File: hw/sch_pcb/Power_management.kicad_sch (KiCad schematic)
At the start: 40 parts

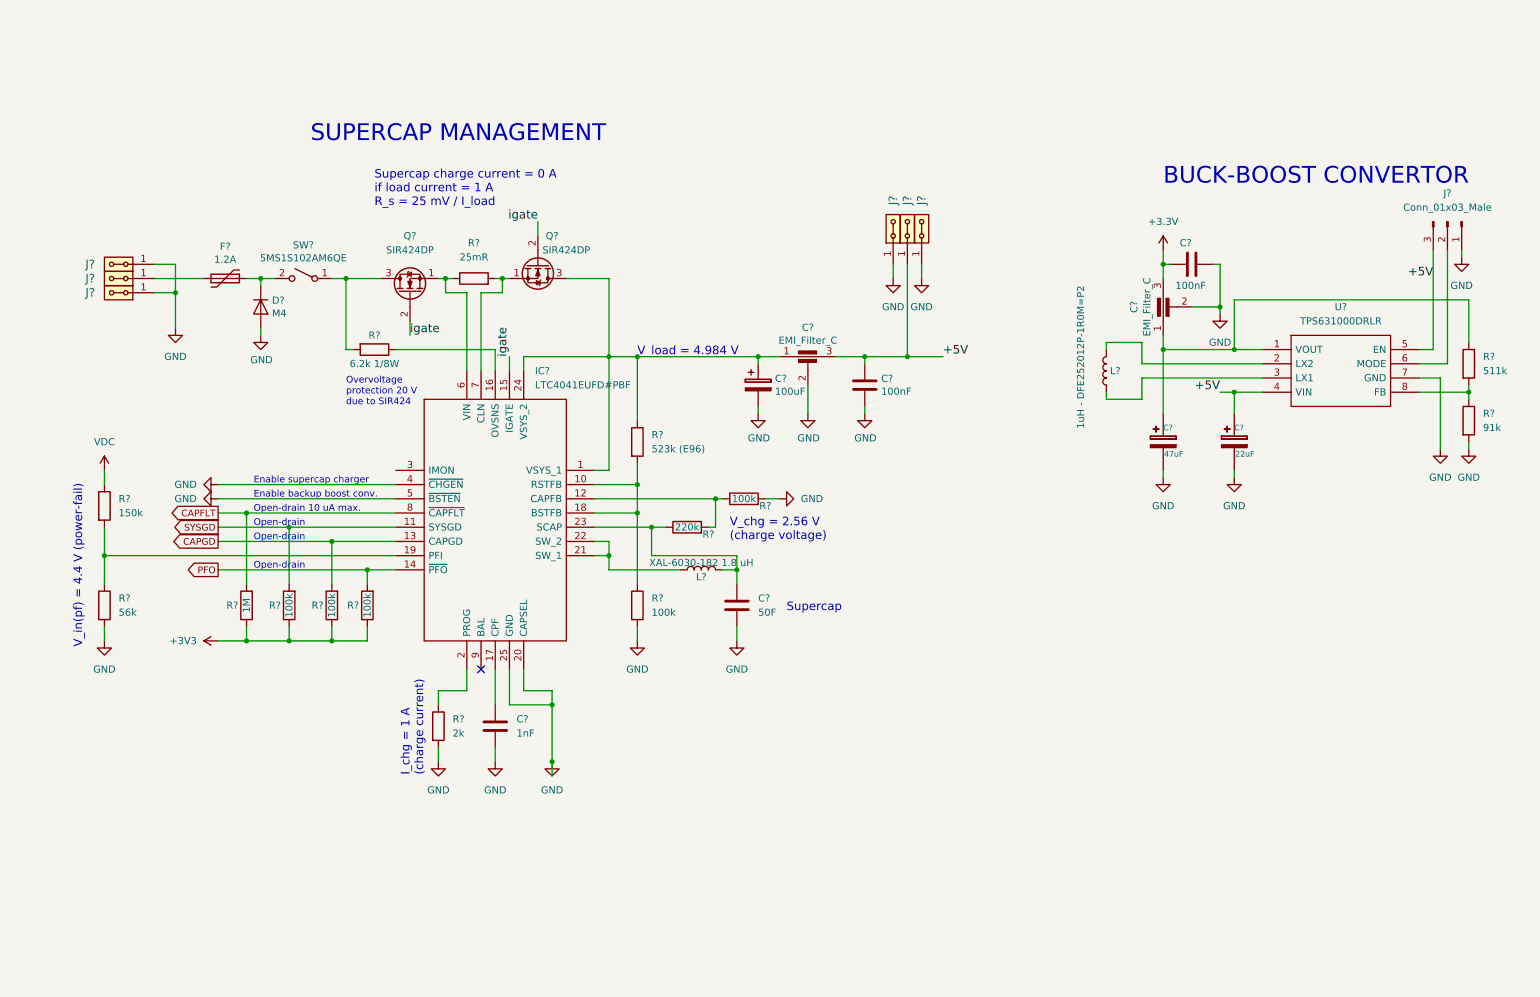
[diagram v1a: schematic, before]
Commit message: schematics update
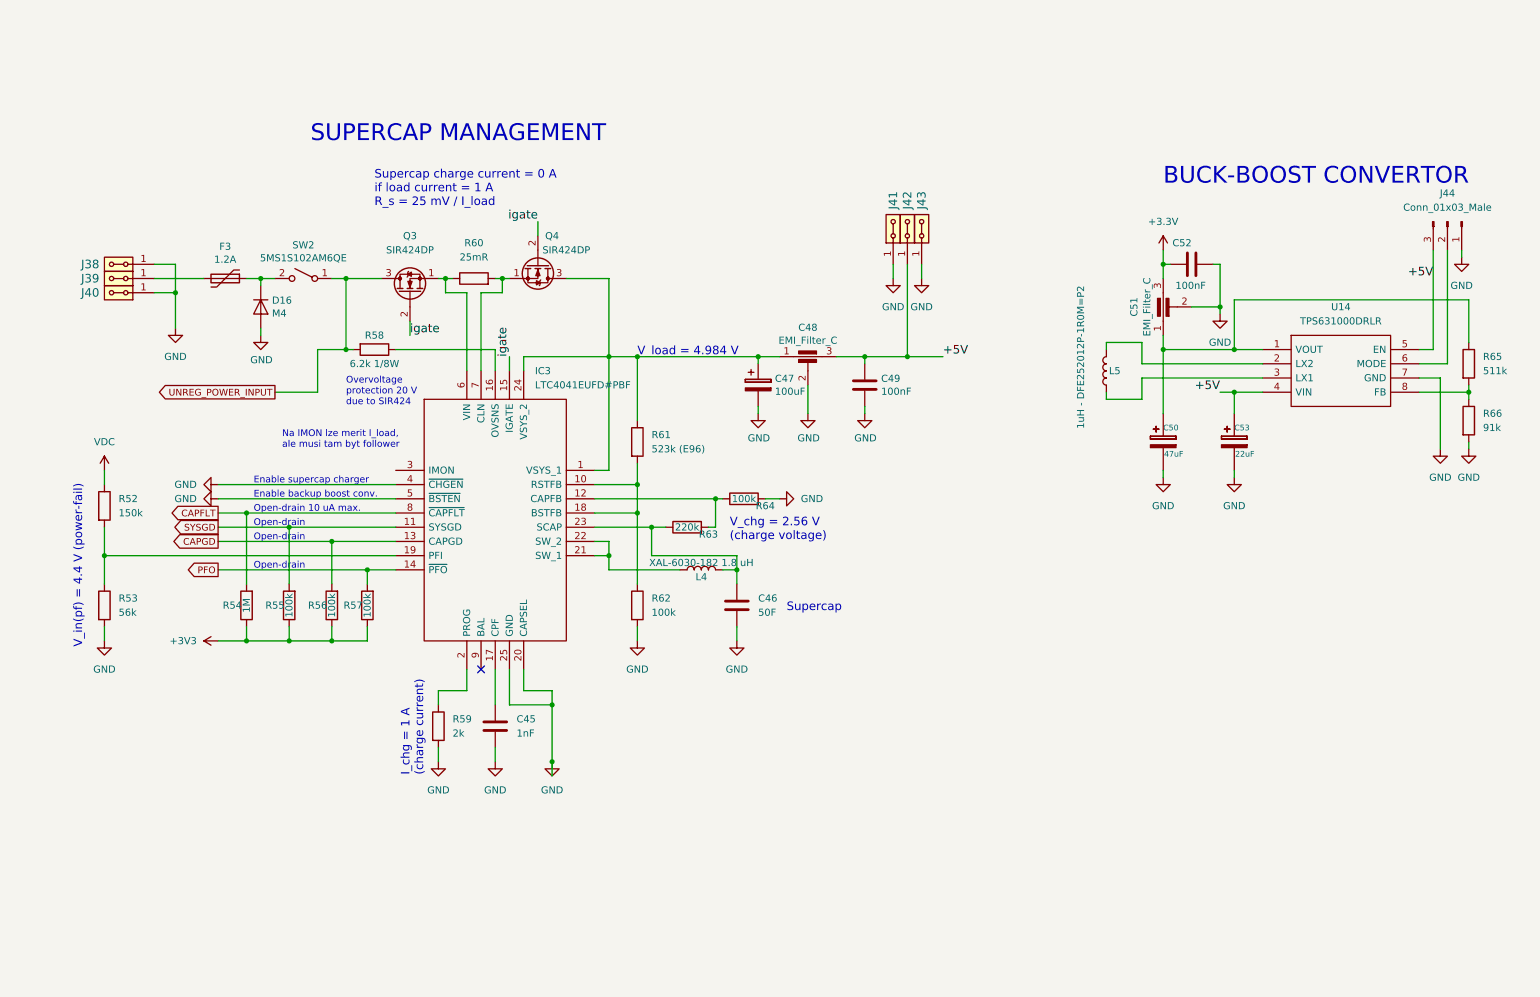
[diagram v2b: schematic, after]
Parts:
- gave numbers to parts that had none: 40
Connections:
- net UNREG_POWER_INPUT: now reaches Q3.3 (D), R58.2, SW2.1 (A)
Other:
- note added: "Na IMON lze merit I_load, ale musi tam byt follower"

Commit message: schematics update
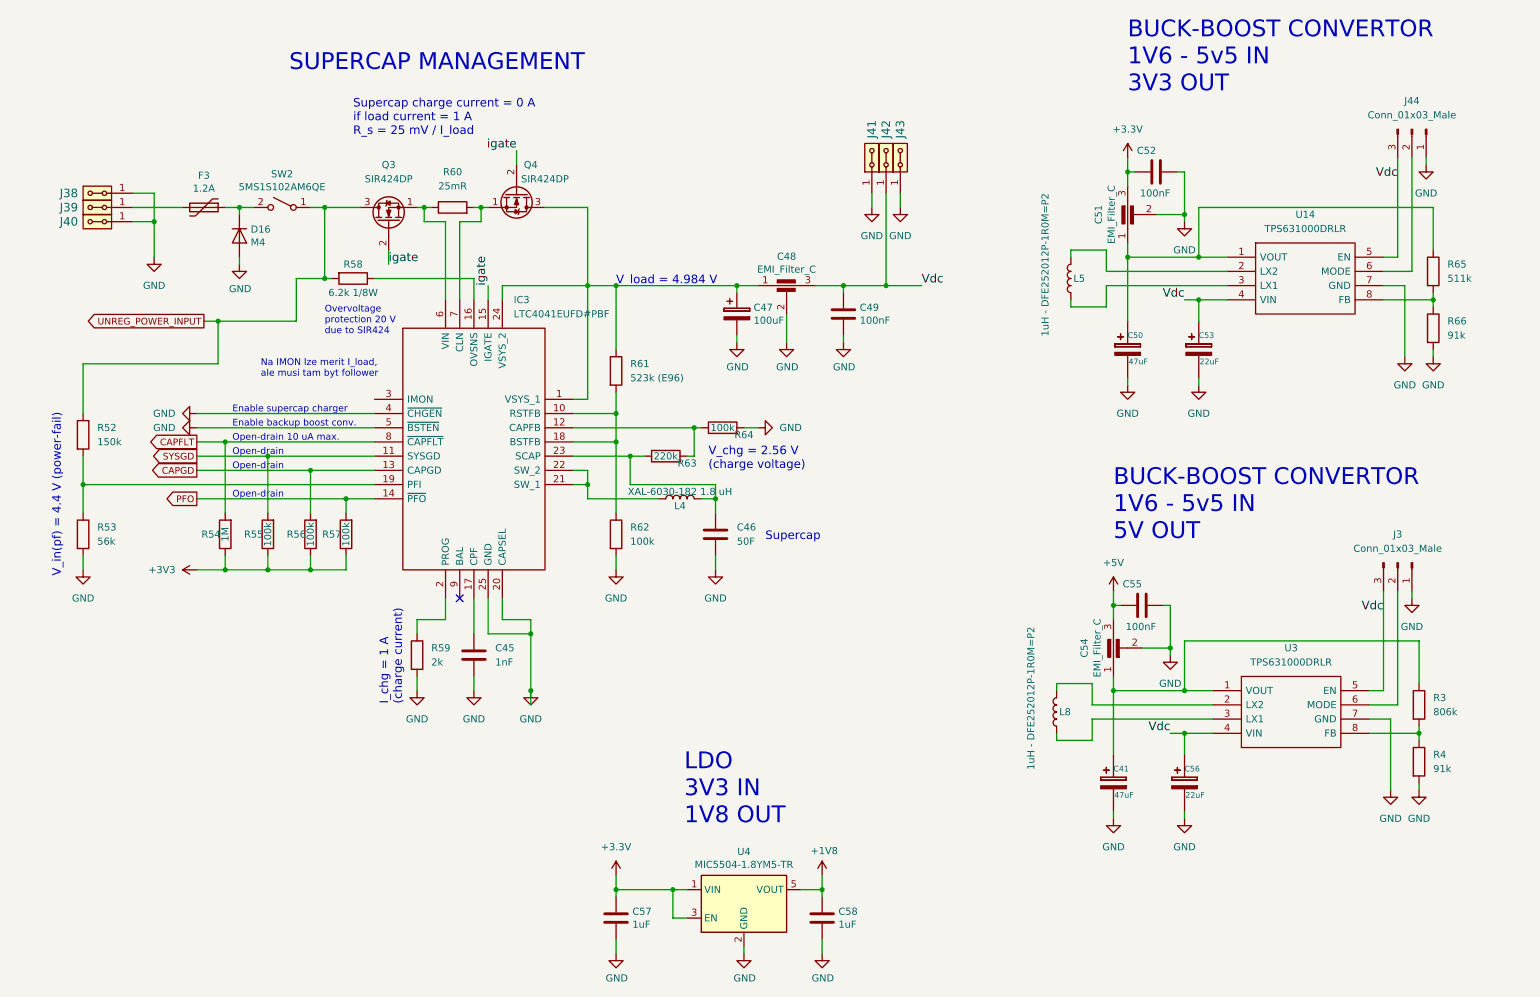
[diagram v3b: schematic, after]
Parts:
- added C41: 47uF, Mlab_C:TantalC_SizeB_Reflow, symbol LION2CELL01D-rescue:CP2
- added C54: EMI_Filter_C, Mlab_L:FIR1, symbol DATALOGGER01A-rescue:EMI_Filter_C-device
- added C55: 100nF, Mlab_R:SMD-0805, symbol DATALOGGER01A-rescue:C-device
- added C56: 22uF, Mlab_C:TantalC_SizeB_Reflow, symbol LION2CELL01D-rescue:CP2
- added C57, C58: 1uF, Mlab_R:SMD-0603, symbol Device:C
- added J3: Conn_01x03_Male, symbol Connector:Conn_01x03_Male
- added L8: 1uH - DFE252012P-1R0M=P2, symbol Device:L
- added R3: 806k, symbol Device:R
- added R4: 91k, symbol Device:R
- added U3: TPS631000DRLR, SOTFL50P160X60-8N, symbol TPS631000DRLR:TPS631000DRLR
- added U4: MIC5504-1.8YM5-TR, Package_TO_SOT_SMD:SOT-23-5, symbol Regulator_Linear:MIC5504-1.8YM5
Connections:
- net VDC is gone; now on net UNREG_POWER_INPUT: R52.1
- net +3.3V: now also C57.1, U4.1 (VIN), U4.3 (EN)
- net +5V: now also C54.3, C55.1; no longer C48.3, C49.1, C53.1, J42.1, J42.2, J44.3 (Pin_3), U14.4 (VIN), U14.5 (EN)
- net GND: now also C41.2, C54.2, C55.2, C56.2, C57.2, C58.2, J3.1 (Pin_1), R4.2, U3.7 (GND), U4.2 (GND)
- new net: C41.1, C54.1, R3.1, U3.1 (VOUT)
- new net: L8.1, U3.3 (LX1)
- new net: L8.2, U3.2 (LX2)
- new net: J3.2 (Pin_2), U3.6 (MODE)
- new net: R3.2, R4.1, U3.8 (FB)
- new net +1V8: C58.1, U4.5 (VOUT)
- new net Vdc: C48.3, C49.1, C53.1, C56.1, J3.3 (Pin_3), J42.1, J42.2, J44.3 (Pin_3), U14.4 (VIN), U14.5 (EN), U3.4 (VIN), U3.5 (EN)
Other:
- note added: "BUCK-BOOST CONVERTOR 1V6 - 5v5 IN 3V3 OUT"
- note added: "BUCK-BOOST CONVERTOR 1V6 - 5v5 IN 5V OUT"
- note added: "LDO 3V3 IN 1V8 OUT"
- note removed: "BUCK-BOOST CONVERTOR"
- moved on the sheet: C45, C46, C47, C48, C49, C50, C51, C52, C53, D16, F3, IC3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

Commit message: progress?
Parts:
- removed J38, J39, J40, J41, J42, J43: HEADER_2x01_PARALLEL, Mlab_Pin_Headers:Straight_2x01, symbol DATALOGGER01A-rescue:HEADER_2x01_PARALLEL-MLAB_HEADER
- removed SW2: 5MS1S102AM6QE, Mlab_SW:5MS1S102AM6QE, symbol Switch:SW_SPST
- added J24, J5: HEADER_2x03_PARALLEL, Mlab_Pin_Headers:Straight_2x03, symbol MLAB_HEADER:HEADER_2x03_PARALLEL
- C26: renamed from C45; footprint (none) -> Mlab_C:SMD-0805
- C27: renamed from C57; footprint Mlab_R:SMD-0603 -> Mlab_C:SMD-0805
- C28: renamed from C46; footprint (none) -> Mlab_C:C_Radial_D16_L25_P7.5
- C30: renamed from C48; footprint Mlab_L:FIR1 -> Mlab_L:FIR_0805
- C31: renamed from C58; footprint Mlab_R:SMD-0603 -> Mlab_C:SMD-0805
- C32: renamed from C49; footprint Mlab_R:SMD-0805 -> Mlab_C:SMD-0805
- C35: renamed from C54; footprint Mlab_L:FIR1 -> Mlab_L:FIR_0805
- C36: renamed from C51; footprint Mlab_L:FIR1 -> Mlab_L:FIR_0805
- C37: renamed from C55; footprint Mlab_R:SMD-0805 -> Mlab_C:SMD-0805
- C38: renamed from C52; footprint Mlab_R:SMD-0805 -> Mlab_C:SMD-0805
- D2: renamed from D16; footprint Mlab_D:SMA_Standard -> Mlab_D:Diode-SMA_Standard
- IC3: footprint QFN50P400X500X80-25N-D -> Package_DFN_QFN:QFN-24-1EP_4x5mm_P0.5mm_EP2.65x3.65mm
- J19: renamed from J3; footprint (none) -> Mlab_Pin_Headers:Straight_1x03
- J20: renamed from J44; footprint (none) -> Mlab_Pin_Headers:Straight_1x03
- L2: renamed from L4; footprint (none) -> XAL6030181MEC:XAL6030181MEC
- L3: renamed from L8; footprint (none) -> Inductor_SMD:L_1008_2520Metric
- L4: renamed from L5; footprint (none) -> Inductor_SMD:L_1008_2520Metric
- Q2: renamed from Q3; footprint Package_TO_SOT_THT:TO-92_Inline -> SIR424DP:SIR106DPT1RE3
- Q3: renamed from Q4; footprint Package_TO_SOT_THT:TO-92_Inline -> SIR424DP:SIR106DPT1RE3
- R29: renamed from R52; footprint (none) -> Mlab_R:SMD-0805
- R30: renamed from R53; footprint (none) -> Mlab_R:SMD-0805
- R31: renamed from R54; footprint (none) -> Mlab_R:SMD-0805
- R32: renamed from R55; footprint (none) -> Mlab_R:SMD-0805
- R33: renamed from R56; footprint (none) -> Mlab_R:SMD-0805
- R34: renamed from R57; footprint (none) -> Mlab_R:SMD-0805
- R35: renamed from R58; footprint (none) -> Mlab_R:SMD-0805
- R36: renamed from R59; footprint (none) -> Mlab_R:SMD-0805
- R37: renamed from R60; footprint (none) -> Mlab_R:SMD-0805
- R38: renamed from R61; footprint (none) -> Mlab_R:SMD-0805
- R39: renamed from R62; footprint (none) -> Mlab_R:SMD-0805
- R40: renamed from R63; footprint (none) -> Mlab_R:SMD-0805
- R41: renamed from R64; footprint (none) -> Mlab_R:SMD-0805
- R42: renamed from R3; footprint (none) -> Mlab_R:SMD-0805
- R43: renamed from R4; footprint (none) -> Mlab_R:SMD-0805
- R44: renamed from R65; footprint (none) -> Mlab_R:SMD-0805
- R45: renamed from R66; footprint (none) -> Mlab_R:SMD-0805
- U10: renamed from U14; footprint SOTFL50P160X60-8N -> Package_TO_SOT_SMD:SOT-583-8
- U9: renamed from U3; footprint SOTFL50P160X60-8N -> Package_TO_SOT_SMD:SOT-583-8
- renumbered C47 to C29, C41 to C33, C50 to C34, C56 to C39, C53 to C40, F3 to F1, U4 to U8
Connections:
- net +3V3 is gone; now on net +3.3V: R31.1, R32.1, R33.1, R34.1
- net GND: now also J24.1, J24.2, J24.5, J24.6, J5.1, J5.2, J5.5, J5.6
- net UNREG_POWER_INPUT: now also D2.1 (K), F1.1
- net Vdc: now also J5.3, J5.4
- net at F1.2: now also J24.3, J24.4
- no-connect marks 1 -> 2
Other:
- note added: "BUCK-BOOST CONVERTOR 1V6 - 5V5 IN 3V3 OUT"
- note added: "BUCK-BOOST CONVERTOR 1V6 - 5V5 IN 5V OUT"
- note removed: "BUCK-BOOST CONVERTOR 1V6 - 5v5 IN 3V3 OUT"
- note removed: "BUCK-BOOST CONVERTOR 1V6 - 5v5 IN 5V OUT"

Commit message: Update components from libraries. Improve schematics. Resolve some ERC and DRC errors.
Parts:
- Q2, Q3: footprint SIR424DP:SIR106DPT1RE3 -> Package_TO_SOT_THT:TO-92_Inline
